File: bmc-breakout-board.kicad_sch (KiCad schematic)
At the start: 5 parts

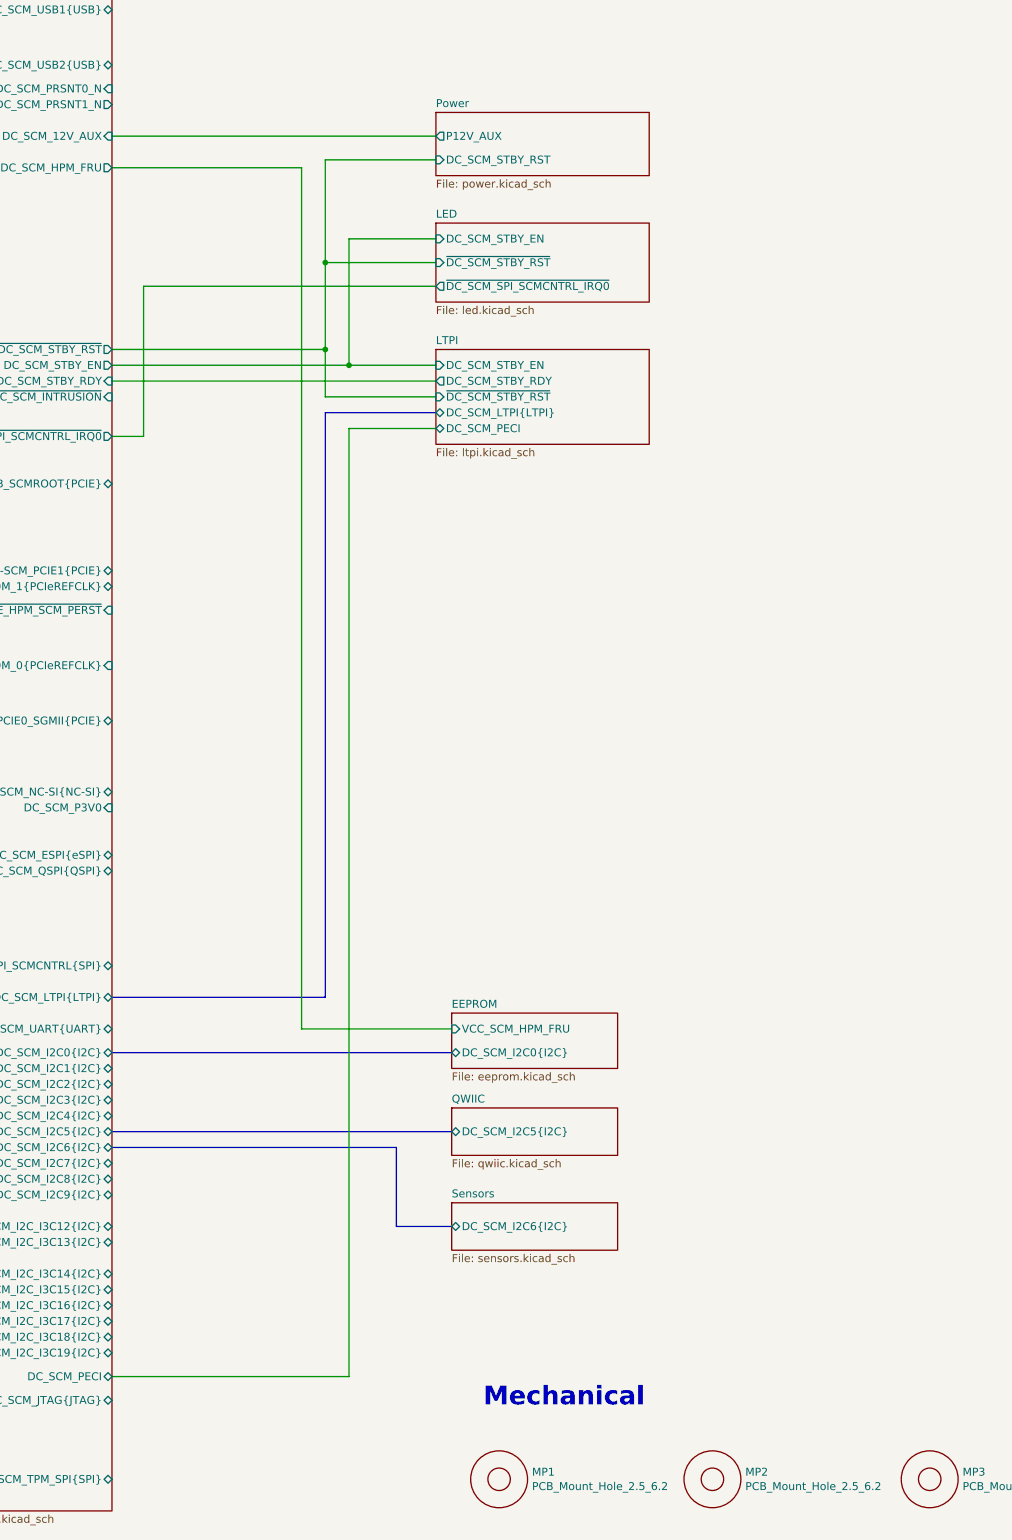
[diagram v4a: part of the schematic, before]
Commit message: [#92504] Add JTAG connector
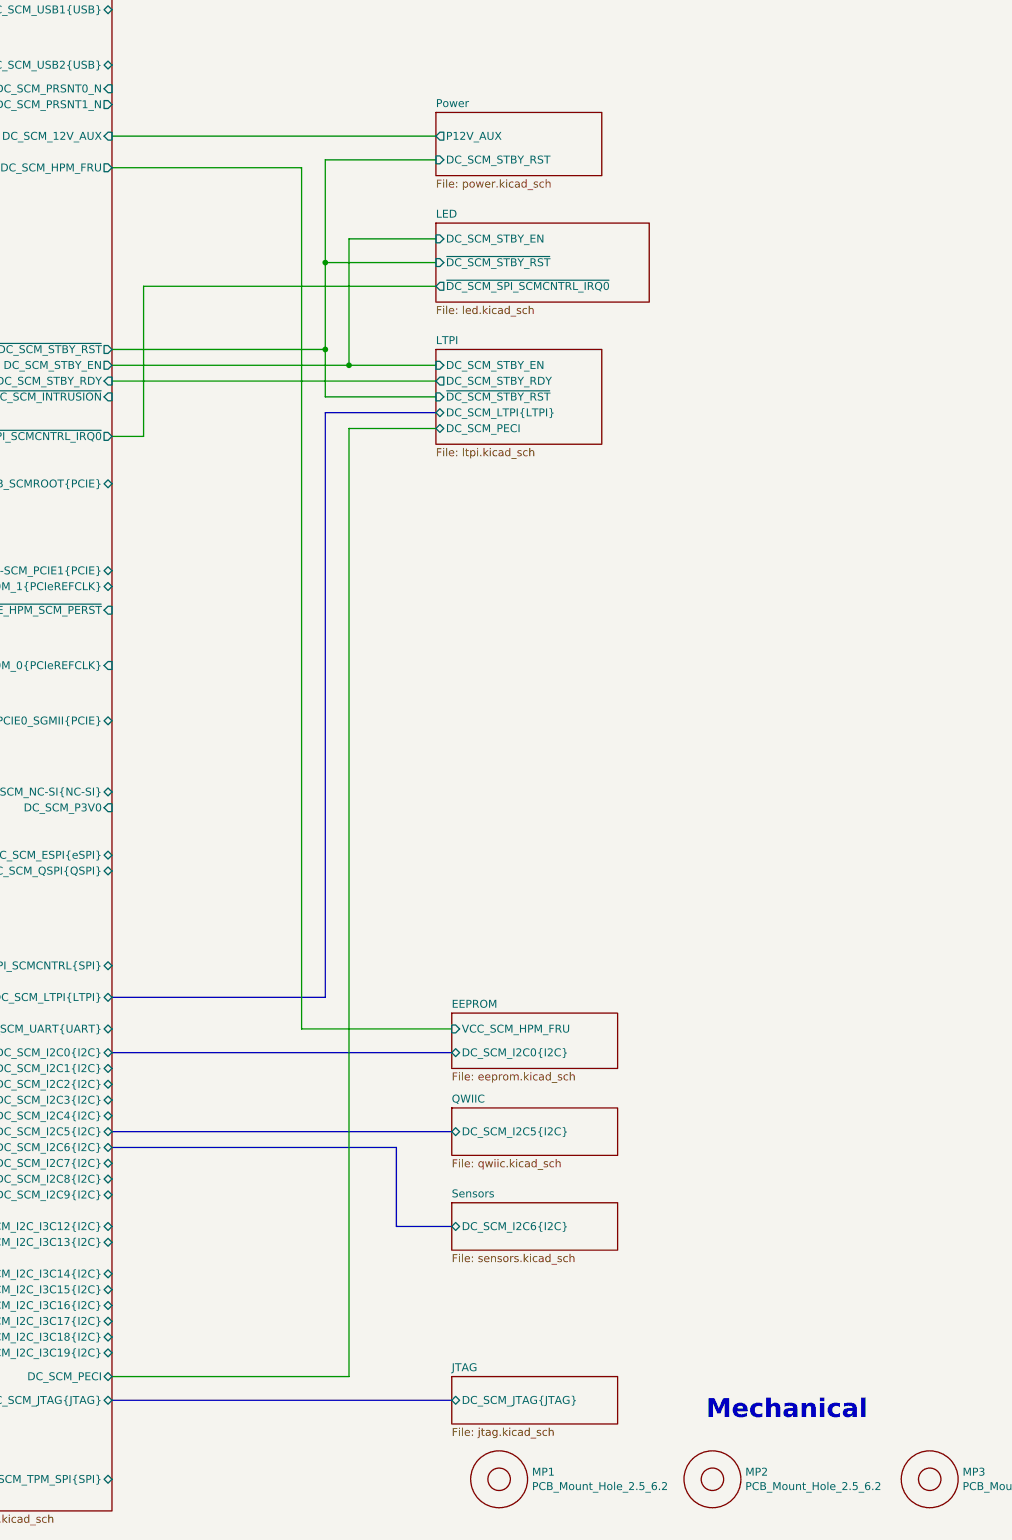
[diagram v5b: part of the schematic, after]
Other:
- added sheet JTAG (jtag.kicad_sch)
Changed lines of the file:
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@@
 	(text "Mechanical"
 		(exclude_from_sim no)
-		(at 116.84 264.16 0)
+		(at 152.654 266.192 0)
 		(effects
 			(font
@@
 	(bus
 		(pts
+			(xy 57.15 262.89) (xy 111.76 262.89)
+		)
+		(stroke
+			(width 0)
+			(type default)
+		)
+	)
+	(bus
+		(pts
 			(xy 57.15 219.71) (xy 111.76 219.71)
 		)
@@
 	(sheet
 		(at 109.22 55.88)
-		(size 34.29 10.16)
+		(size 26.67 10.16)
 		(exclude_from_sim no)
 		(in_bom yes)
@@
 	(sheet
 		(at 109.22 93.98)
-		(size 34.29 15.24)
+		(size 26.67 15.24)
 		(exclude_from_sim no)
 		(in_bom yes)
@@
 				)
 			)
+		)
+	)
+	(sheet
+		(at 111.76 259.08)
+		(size 26.67 7.62)
+		(exclude_from_sim no)
+		(in_bom yes)
+		(on_board yes)
+		(dnp no)
+		(fields_autoplaced yes)
+		(stroke
+			(width 0.1524)
+			(type solid)
+		)
+		(fill
+			(color 0 0 0 0.0000)
+		)
+		(property "Sheetname" "JTAG"
+			(at 111.76 258.3684 0)
+			(effects
+				(font
+					(size 1.27 1.27)
+				)
+				(justify left bottom)
+			)
+		)
+		(property "Sheetfile" "jtag.kicad_sch"
+			(at 111.76 267.2846 0)
+			(effects
+				(font
+					(size 1.27 1.27)
+				)
+				(justify left top)
+			)
+		)
+		(pin "DC_SCM_JTAG{JTAG}" bidirectional
+			(at 111.76 262.89 180)
+			(effects
+				(font
+					(size 1.27 1.27)
+				)
+				(justify left)
+			)
+		)
+		(instances
+			(project "bmc-breakout-board"
+				(path "/5d67ef28-5805-4f87-b722-2926dabf7f6e"
+					(page "9")
+				)
+			)

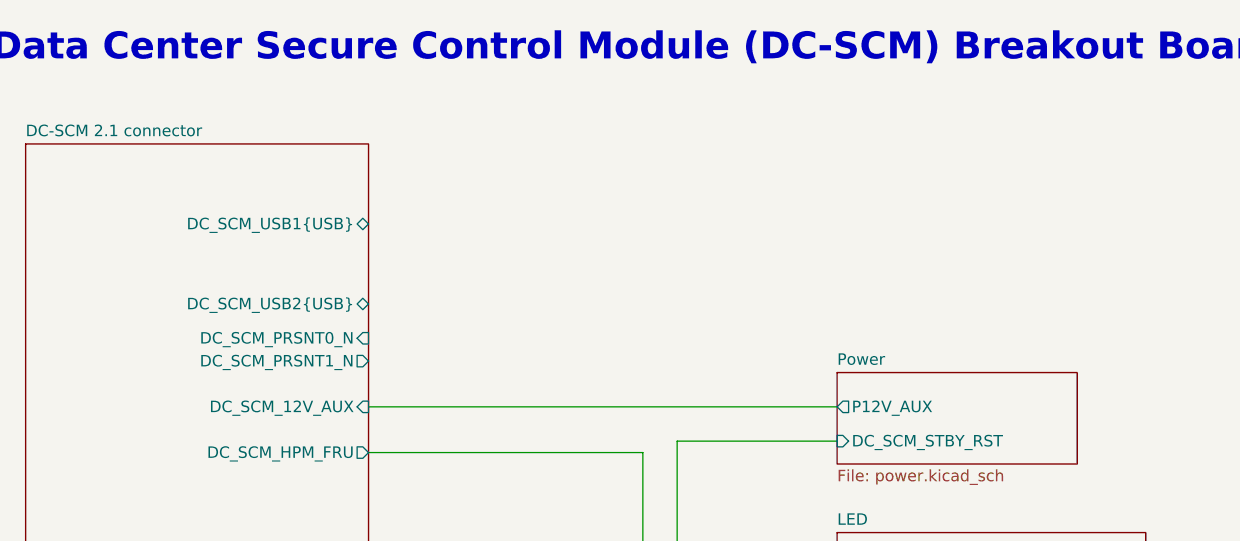
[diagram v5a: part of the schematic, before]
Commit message: [#92504] Add HOST USB type A
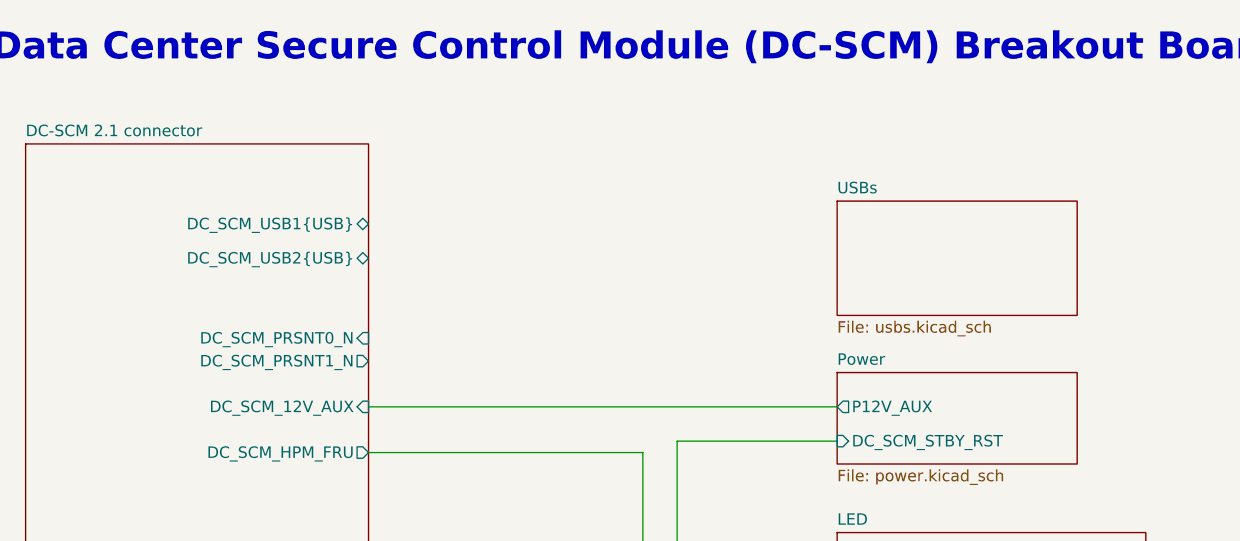
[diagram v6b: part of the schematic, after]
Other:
- added sheet USBs (usbs.kicad_sch)
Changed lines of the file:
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@@
+	)
+	(sheet
+		(at 109.22 36.83)
+		(size 26.67 12.7)
+		(exclude_from_sim no)
+		(in_bom yes)
+		(on_board yes)
+		(dnp no)
+		(fields_autoplaced yes)
+		(stroke
+			(width 0.1524)
+			(type solid)
+		)
+		(fill
+			(color 0 0 0 0.0000)
+		)
+		(property "Sheetname" "USBs"
+			(at 109.22 36.1184 0)
+			(effects
+				(font
+					(size 1.27 1.27)
+				)
+				(justify left bottom)
+			)
+		)
+		(property "Sheetfile" "usbs.kicad_sch"
+			(at 109.22 50.1146 0)
+			(effects
+				(font
+					(size 1.27 1.27)
+				)
+				(justify left top)
+			)
+		)
+		(instances
+			(project "bmc-breakout-board"
+				(path "/5d67ef28-5805-4f87-b722-2926dabf7f6e"
+					(page "10")
+				)
+			)
+		)
 	)
 	(sheet
@@
 		)
 		(pin "DC_SCM_USB2{USB}" bidirectional
-			(at 57.15 48.26 0)
-			(effects
-				(font
+			(at 57.15 43.18 0)
+			(effects
+				(font

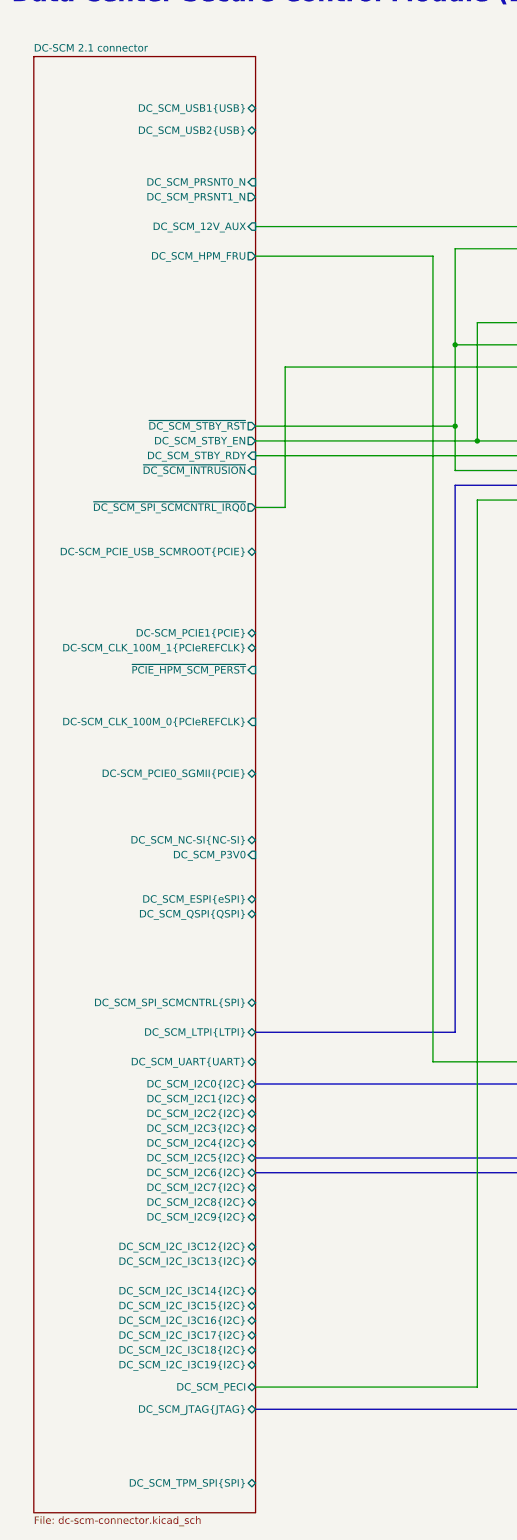
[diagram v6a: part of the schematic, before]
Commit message: [#92504] Clear Wire BUS errors
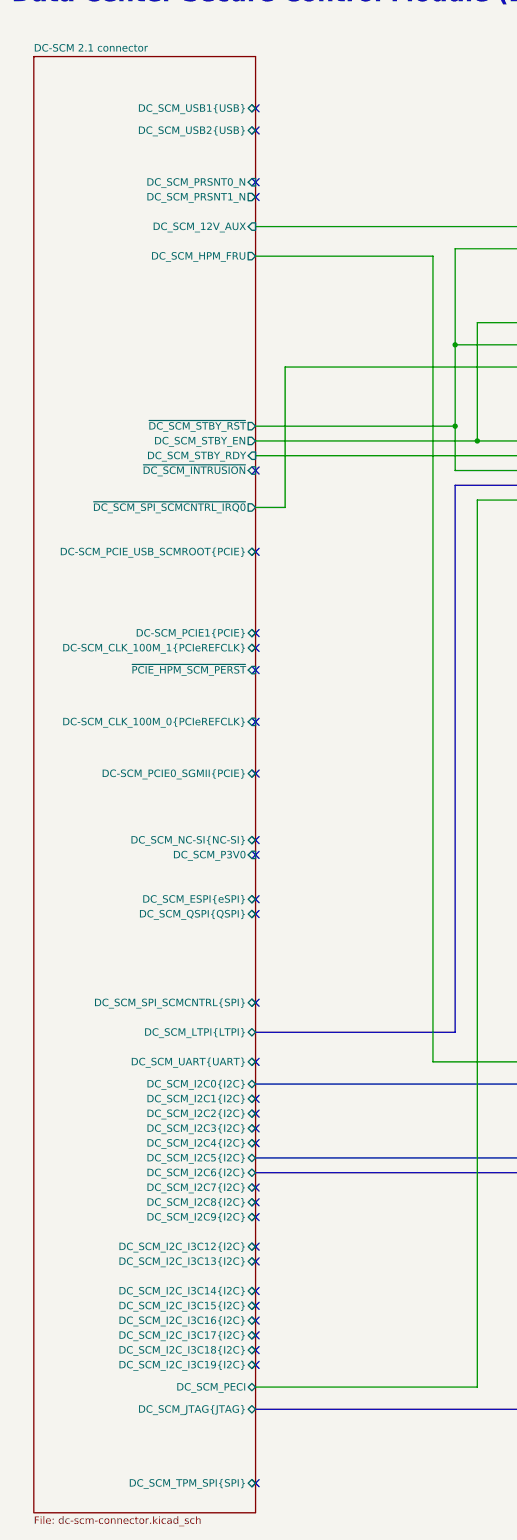
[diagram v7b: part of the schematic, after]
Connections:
- no-connect marks 0 -> 33
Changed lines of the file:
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@@
 		(color 0 0 0 0)
+	)
+	(no_connect
+		(at 57.15 212.09)
+	)
+	(no_connect
+		(at 57.15 224.79)
+	)
+	(no_connect
+		(at 57.15 144.78)
+	)
+	(no_connect
+		(at 57.15 245.11)
+	)
+	(no_connect
+		(at 57.15 275.59)
+	)
+	(no_connect
+		(at 57.15 153.67)
+	)
+	(no_connect
+		(at 57.15 193.04)
+	)
+	(no_connect
+		(at 57.15 214.63)
+	)
+	(no_connect
+		(at 57.15 54.61)
+	)
+	(no_connect
+		(at 57.15 129.54)
+	)
+	(no_connect
+		(at 57.15 242.57)
+	)
+	(no_connect
+		(at 57.15 167.64)
+	)
+	(no_connect
+		(at 57.15 217.17)
+	)
+	(no_connect
+		(at 57.15 39.37)
+	)
+	(no_connect
+		(at 57.15 255.27)
+	)
+	(no_connect
+		(at 57.15 234.95)
+	)
+	(no_connect
+		(at 57.15 135.89)
+	)
+	(no_connect
+		(at 57.15 203.2)
+	)
+	(no_connect
+		(at 57.15 52.07)
+	)
+	(no_connect
+		(at 57.15 250.19)
+	)
+	(no_connect
+		(at 57.15 132.08)
+	)
+	(no_connect
+		(at 57.15 101.6)
+	)
+	(no_connect
+		(at 57.15 227.33)
+	)
+	(no_connect
+		(at 57.15 165.1)
+	)
+	(no_connect
+		(at 57.15 115.57)
+	)
+	(no_connect
+		(at 57.15 209.55)
+	)
+	(no_connect
+		(at 57.15 177.8)
+	)
+	(no_connect
+		(at 57.15 237.49)
+	)
+	(no_connect
+		(at 57.15 43.18)
+	)
+	(no_connect
+		(at 57.15 247.65)
+	)
+	(no_connect
+		(at 57.15 229.87)
+	)
+	(no_connect
+		(at 57.15 175.26)
+	)
+	(no_connect
+		(at 57.15 252.73)
 	)
 	(bus

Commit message: [#92504] Connect USBs
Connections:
- no-connect marks 33 -> 30
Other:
- sheet USBs ports: added DC_SCM_UART{UART}, DC_SCM_USB1{USB}, DC_SCM_USB2{USB}; removed none
- moved on the sheet: MP1, MP2, MP3
